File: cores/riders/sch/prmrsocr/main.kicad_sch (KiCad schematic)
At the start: 27 parts

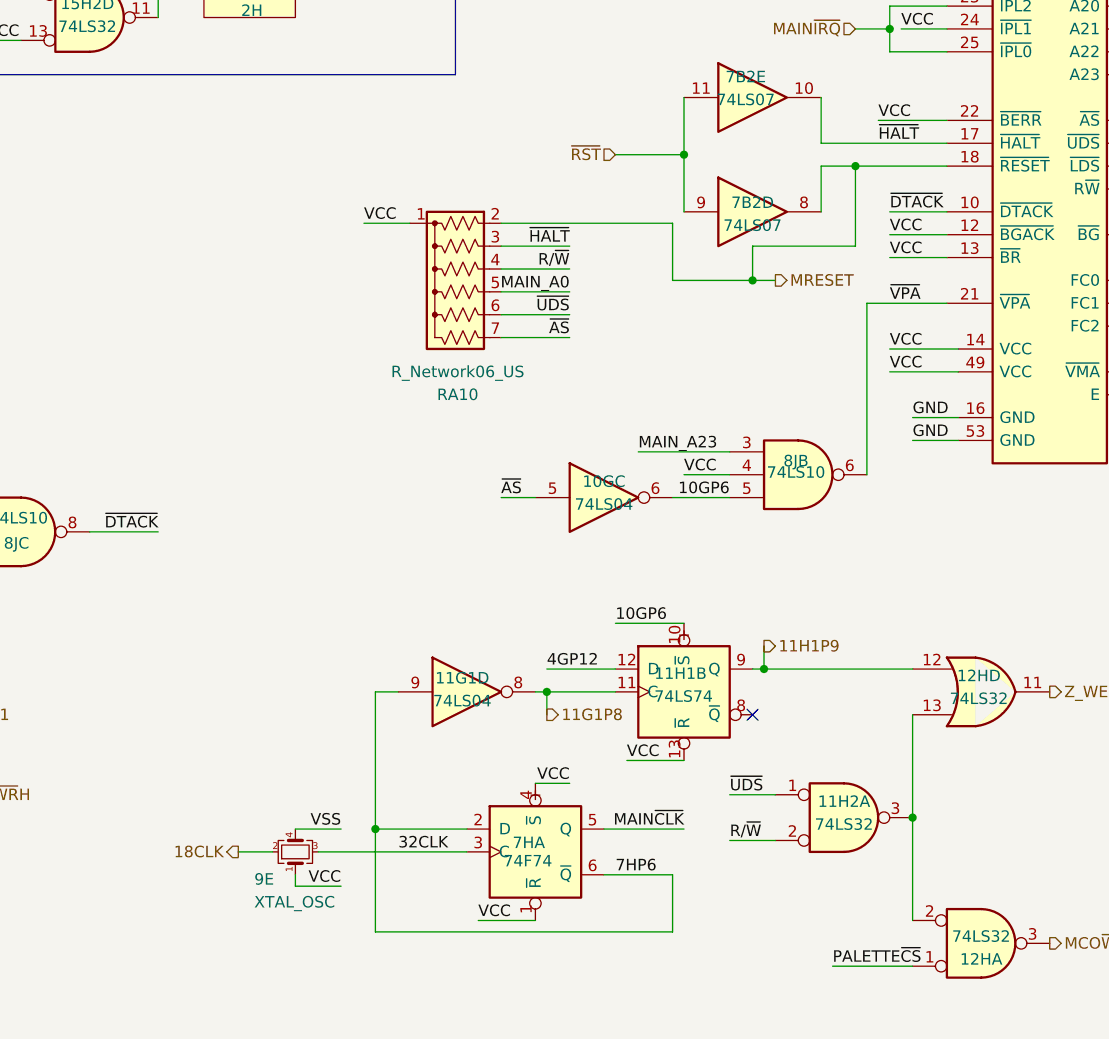
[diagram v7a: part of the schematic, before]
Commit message: prmrsocr: 054986 sheet complete and fixes
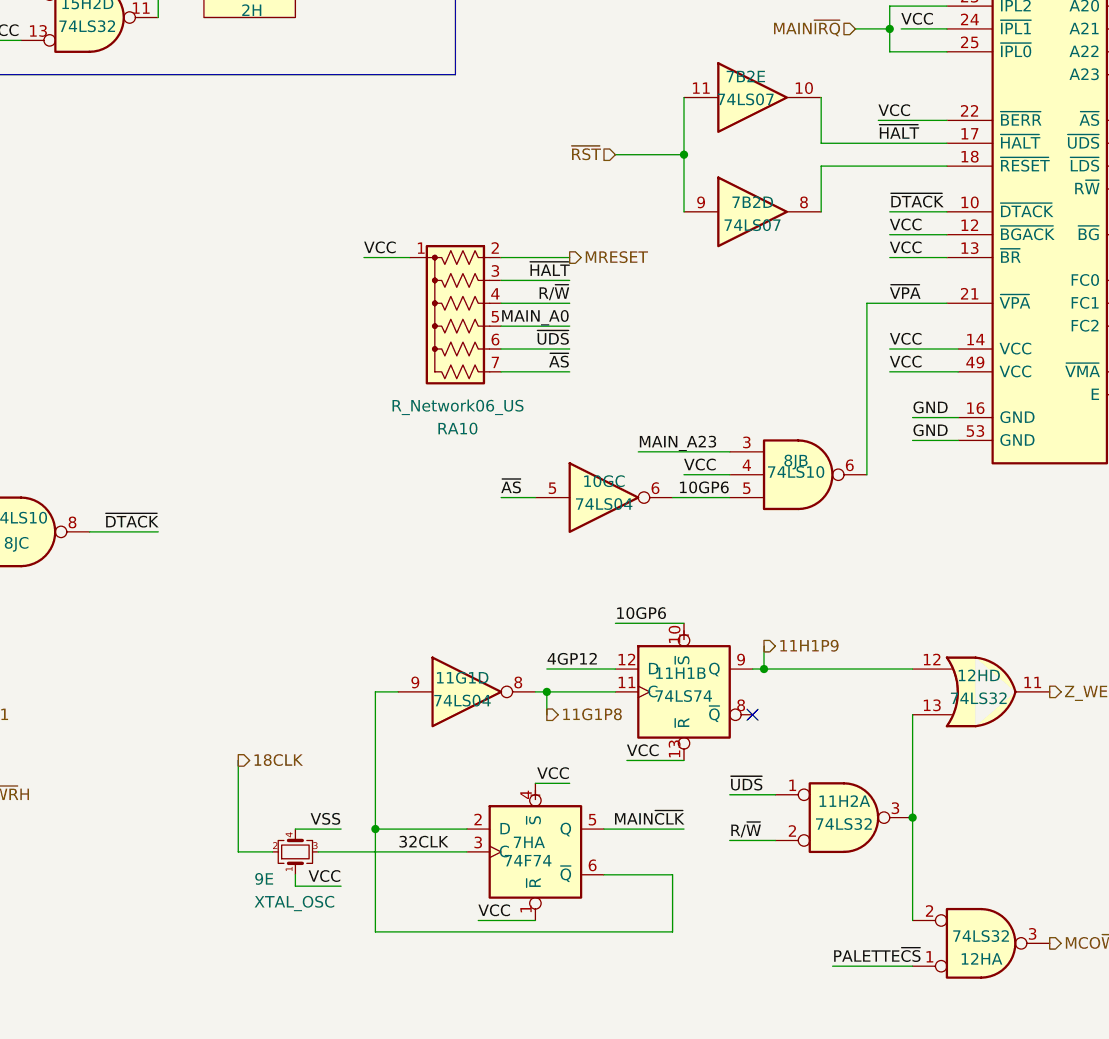
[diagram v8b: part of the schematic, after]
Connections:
- net MRESET: no longer 6H.18 (~{RESET}), 7B2.8
- net 7HP6: no longer names the net of 11G1.9, 7H.2 (D), 7H.6 (~{Q})
- new net: 6H.18 (~{RESET}), 7B2.8
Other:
- moved on the sheet: RA10
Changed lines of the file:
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@@
 	)
 	(junction
-		(at 205.74 92.71)
-		(diameter 0)
-		(color 0 0 0 0)
-	)
-	(junction
 		(at 67.31 156.21)
 		(diameter 0)
@@
 	)
 	(junction
-		(at 194.31 105.41)
-		(diameter 0)
-		(color 0 0 0 0)
-	)
-	(junction
 		(at 186.69 91.44)
 		(diameter 0)
@@
 	(wire
 		(pts
-			(xy 205.74 92.71) (xy 215.9 92.71)
+			(xy 201.93 92.71) (xy 215.9 92.71)
 		)
 		(stroke
@@
 	(wire
 		(pts
-			(xy 196.85 105.41) (xy 194.31 105.41)
+			(xy 137.16 168.91) (xy 140.97 168.91)
+		)
+		(stroke
+			(width 0)
+			(type default)
+		)
+	)
+	(wire
+		(pts
+			(xy 173.99 102.87) (xy 166.37 102.87)
 		)
 		(stroke
@@
 	(wire
 		(pts
-			(xy 173.99 106.68) (xy 166.37 106.68)
+			(xy 173.99 110.49) (xy 166.37 110.49)
 		)
 		(stroke
@@
 	(wire
 		(pts
-			(xy 166.37 104.14) (xy 173.99 104.14)
+			(xy 166.37 107.95) (xy 173.99 107.95)
 		)
 		(stroke
@@
 	(wire
 		(pts
-			(xy 137.16 168.91) (xy 140.97 168.91)
-		)
-		(stroke
-			(width 0)
-			(type default)
-		)
-	)
-	(wire
-		(pts
 			(xy 77.47 156.21) (xy 87.63 156.21)
 		)
@@
 	(wire
 		(pts
-			(xy 173.99 109.22) (xy 166.37 109.22)
+			(xy 173.99 113.03) (xy 166.37 113.03)
 		)
 		(stroke
@@
 	(wire
 		(pts
-			(xy 173.99 111.76) (xy 166.37 111.76)
+			(xy 173.99 115.57) (xy 166.37 115.57)
 		)
 		(stroke
@@
 		)
 	)
-	(wire
-		(pts
-			(xy 194.31 105.41) (xy 194.31 101.6)
-		)
-		(stroke
-			(width 0)
-			(type default)
-		)
-	)
 	(bus
 		(pts
@@
 	(wire
 		(pts
-			(xy 151.13 99.06) (xy 156.21 99.06)
+			(xy 151.13 102.87) (xy 156.21 102.87)
 		)
 		(stroke
@@
 	(wire
 		(pts
-			(xy 194.31 105.41) (xy 185.42 105.41)
-		)
-		(stroke
-			(width 0)
-			(type default)
-		)
-	)
-	(wire
-		(pts
 			(xy 180.34 158.75) (xy 186.69 158.75)
 		)
@@
 	(wire
 		(pts
-			(xy 205.74 101.6) (xy 205.74 92.71)
-		)
-		(stroke
-			(width 0)
-			(type default)
-		)
-	)
-	(wire
-		(pts
 			(xy 209.55 80.01) (xy 215.9 80.01)
 		)
@@
 	(wire
 		(pts
-			(xy 173.99 101.6) (xy 166.37 101.6)
+			(xy 173.99 105.41) (xy 166.37 105.41)
 		)
 		(stroke
@@
 	(wire
 		(pts
-			(xy 270.51 74.93) (xy 280.67 74.93)
+			(xy 137.16 158.75) (xy 137.16 168.91)
 		)
 		(stroke
@@
 	(wire
 		(pts
-			(xy 185.42 99.06) (xy 166.37 99.06)
+			(xy 270.51 74.93) (xy 280.67 74.93)
 		)
 		(stroke
@@
 	(wire
 		(pts
-			(xy 201.93 92.71) (xy 205.74 92.71)
-		)
-		(stroke
-			(width 0)
-			(type default)
-		)
-	)
-	(wire
-		(pts
 			(xy 158.75 33.02) (xy 148.59 33.02)
 		)
@@
 	(wire
 		(pts
-			(xy 290.83 26.67) (xy 290.83 29.21)
-		)
-		(stroke
-			(width 0)
-			(type default)
-		)
-	)
-	(bus
-		(pts
-			(xy 267.97 57.15) (xy 267.97 59.69)
+			(xy 186.69 91.44) (xy 186.69 97.79)
 		)
 		(stroke
@@
 	(wire
 		(pts
-			(xy 212.09 153.67) (xy 212.09 165.1)
+			(xy 290.83 26.67) (xy 290.83 29.21)
 		)
 		(stroke
@@
 		)
 	)
-	(wire
+	(bus
 		(pts
-			(xy 163.83 176.53) (xy 170.18 176.53)
+			(xy 267.97 57.15) (xy 267.97 59.69)
 		)
 		(stroke
@@
 	(wire
 		(pts
-			(xy 186.69 91.44) (xy 186.69 97.79)
+			(xy 212.09 153.67) (xy 212.09 165.1)
 		)
 		(stroke
@@
 	(wire
 		(pts
-			(xy 194.31 101.6) (xy 205.74 101.6)
+			(xy 163.83 176.53) (xy 170.18 176.53)
 		)
 		(stroke
@@
 		)
 	)
-	(wire
-		(pts
-			(xy 185.42 105.41) (xy 185.42 99.06)
-		)
-		(stroke
-			(width 0)
-			(type default)
-		)
-	)
 	(bus
 		(pts
@@
 	)
 	(label "~{AS}"
-		(at 173.99 111.76 180)
+		(at 173.99 115.57 180)
 		(effects
 			(font
@@
 	)
 	(label "R{slash}~{W}"
-		(at 173.99 104.14 180)
+		(at 173.99 107.95 180)
 		(effects
 			(font
@@
 	)
 	(label "MAIN_A0"
-		(at 173.99 106.68 180)
+		(at 173.99 110.49 180)
 		(effects
 			(font
@@
 	)
 	(label "~{HALT}"
-		(at 173.99 101.6 180)
+		(at 173.99 105.41 180)
 		(effects
 			(font
@@
 	)
 	(label "VCC"
-		(at 151.13 99.06 0)
+		(at 151.13 102.87 0)
 		(effects
 			(font
@@
 		)
 	)
-	(label "7HP6"
-		(at 179.07 171.45 0)
-		(effects
-			(font
-				(size 1.27 1.27)
-			)
-			(justify left bottom)
-		)
-	)
 	(label "10GP6"
 		(at 270.51 113.03 0)
@@
 	)
 	(label "~{UDS}"
-		(at 173.99 109.22 180)
+		(at 173.99 113.03 180)
 		(effects
 			(font
@@
 		)
 	)
-	(hierarchical_label "MRESET"
-		(shape output)
-		(at 196.85 105.41 0)
-		(effects
-			(font
-				(size 1.27 1.27)
-			)
-			(justify left)
-		)
-	)
 	(hierarchical_label "MAIN_A[19..0]"
 		(shape output)
@@
 		)
 	)
+	(hierarchical_label "MRESET"
+		(shape output)
+		(at 173.99 102.87 0)
+		(effects
+			(font
+				(size 1.27 1.27)
+			)
+			(justify left)
+		)
+	)
 	(hierarchical_label "IOCS"
 		(shape output)
@@
 	(hierarchical_label "18CLK"
 		(shape output)
-		(at 137.16 168.91 180)
+		(at 137.16 158.75 0)
 		(effects
 			(font
 				(size 1.27 1.27)
 			)
-			(justify right)
+			(justify left)
 		)
 	)
@@
 	(symbol
 		(lib_id "Device:R_Network06_US")
-		(at 161.29 106.68 90)
+		(at 161.29 110.49 90)
 		(mirror x)
 		(unit 1)
@@
 		(fields_autoplaced yes)
 		(property "Reference" "RA10"
-			(at 161.544 118.11 90)
+			(at 161.544 121.92 90)
 			(effects
 				(font
@@
 		)
 		(property "Value" "R_Network06_US"
-			(at 161.544 115.57 90)
+			(at 161.544 119.38 90)
 			(effects
 				(font
@@
 		)
 		(property "Footprint" "Resistor_THT:R_Array_SIP7"
-			(at 161.29 116.205 90)
+			(at 161.29 120.015 90)
 			(effects
 				(font
@@
 		)
 		(property "Datasheet" "http://www.vishay.com/docs/31509/csc.pdf"
-			(at 161.29 106.68 0)
+			(at 161.29 110.49 0)
 			(effects
 				(font
@@
 		)
 		(property "Description" "6 resistor network, star topology, bussed resistors, small US symbol"
-			(at 161.29 106.68 0)
+			(at 161.29 110.49 0)
 			(effects
 				(font
